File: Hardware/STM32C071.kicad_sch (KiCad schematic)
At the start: 15 parts, among them J1 USB_C_Receptacle_USB2.0_16P, U1 STM32C071K8Tx, U2 USBLC6-2P6, U4 XL1509-ADJE1

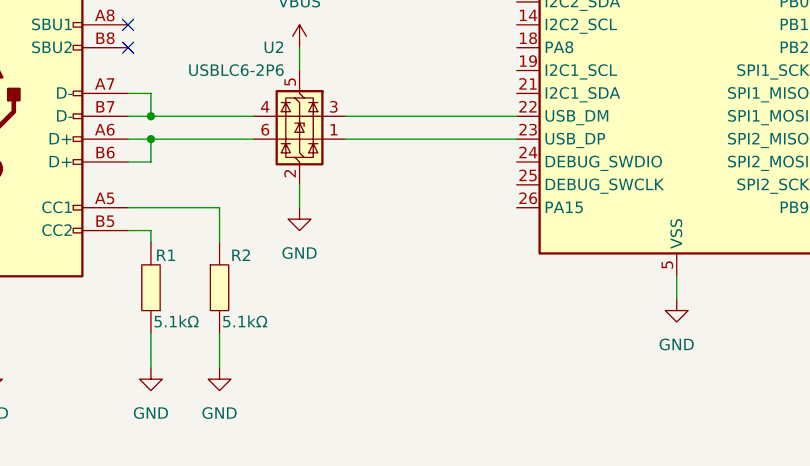
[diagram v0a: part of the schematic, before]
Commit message: Added SWD connector and 3D view
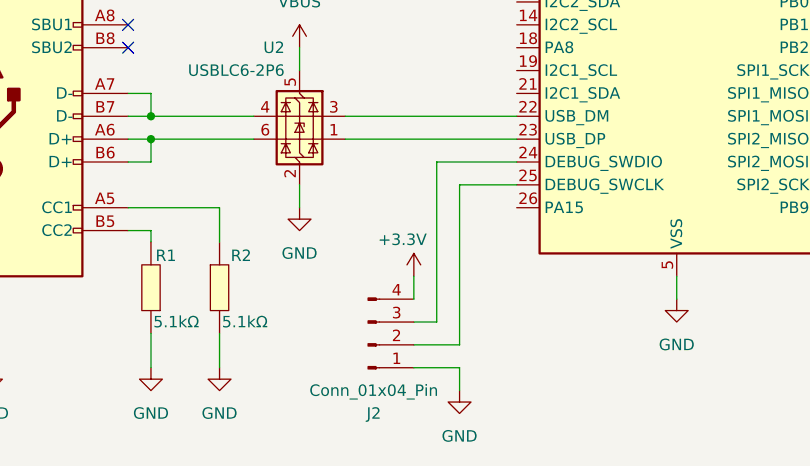
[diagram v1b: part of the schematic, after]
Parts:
- added J2: Conn_01x04_Pin, Connector_PinHeader_2.54mm:PinHeader_1x04_P2.54mm_Horizontal, symbol Connector:Conn_01x04_Pin
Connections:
- net +3.3V: now also J2.4 (Pin_4)
- net GND: now also J2.1 (Pin_1)
- net at U1.24 (PA13): now also J2.3 (Pin_3)
- net at U1.25 (PA14): now also J2.2 (Pin_2)

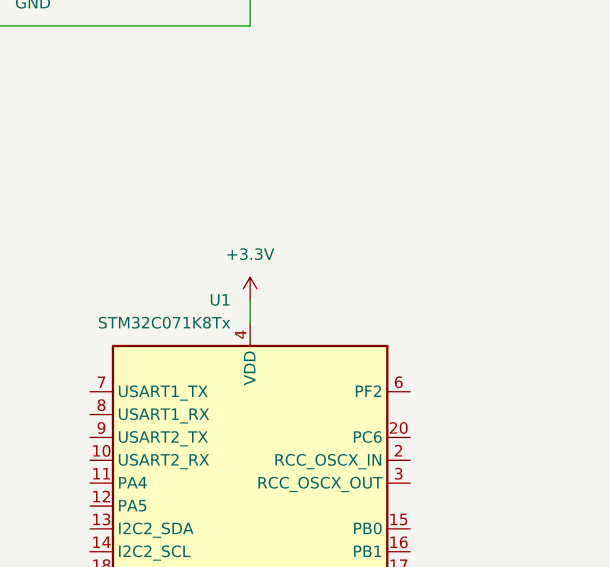
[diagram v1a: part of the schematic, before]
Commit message: Added Reset and power connections, 45 rotation
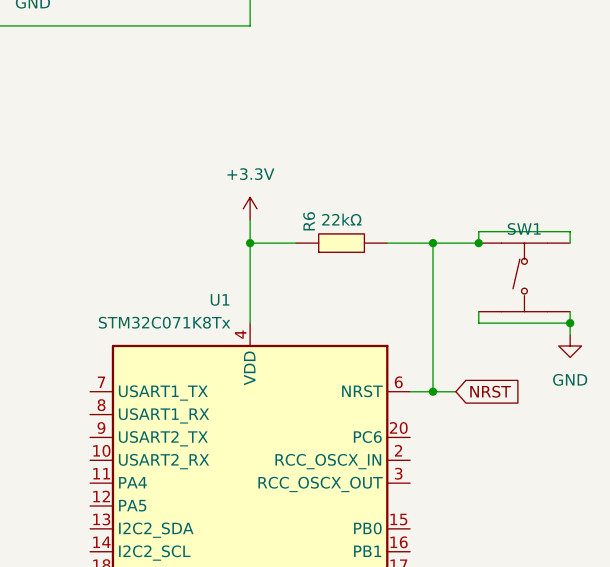
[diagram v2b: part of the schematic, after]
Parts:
- added R6: 22kΩ, jlcbasic:R0805, symbol jlcbasic:22kΩ-0805
- added SW1: TS-1187A-B-A-B, jlcbasic:SW-SMD_4P-L5.1-W5.1-P3.70-LS6.5-TL_H1.5, symbol jlcbasic:TS-1187A-B-A-B
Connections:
- net +3.3V: now also R6.1
- net GND: now also SW1.3 (C), SW1.4 (D)
- net NRST: now reaches U1.6 (PF2)
- net NRST: now also R6.2, SW1.1 (A), SW1.2 (B)
